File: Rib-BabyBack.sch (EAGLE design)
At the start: 30 parts, among them IC1 REG1117, SW1 DPDT

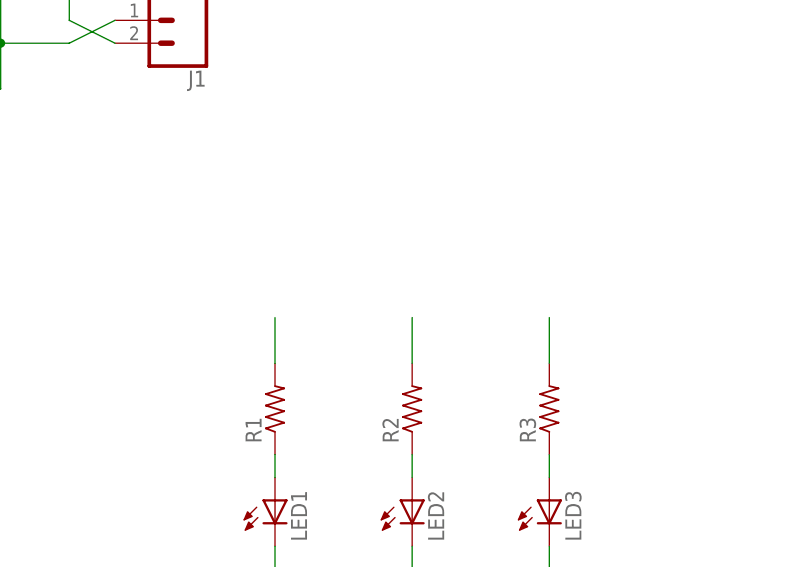
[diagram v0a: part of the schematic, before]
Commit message: Resolved issue 38
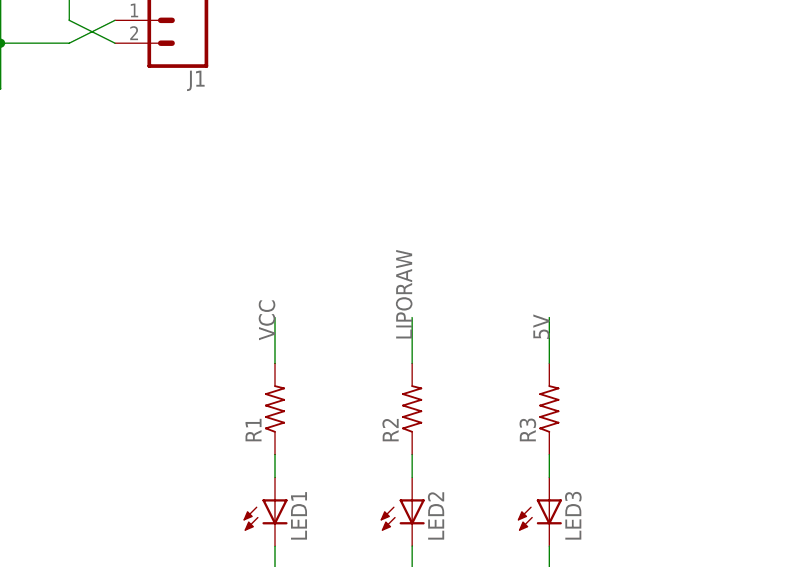
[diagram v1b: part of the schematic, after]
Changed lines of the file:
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@@
 <pinref part="R1" gate="G$1" pin="2"/>
 <wire x1="96.52" y1="-96.52" x2="96.52" y2="-91.44" width="0.1524" layer="91"/>
+<label x="96.52" y="-93.98" size="1.778" layer="95" rot="R90"/>
 </segment>
 </net>
@@
 <pinref part="R3" gate="G$1" pin="2"/>
 <wire x1="127" y1="-96.52" x2="127" y2="-91.44" width="0.1524" layer="91"/>
+<label x="127" y="-93.98" size="1.778" layer="95" rot="R90"/>
 </segment>
 <segment>
@@
 <pinref part="R2" gate="G$1" pin="2"/>
 <wire x1="111.76" y1="-96.52" x2="111.76" y2="-91.44" width="0.1524" layer="91"/>
+<label x="111.76" y="-93.98" size="1.778" layer="95" rot="R90"/>
 </segment>
 </net>

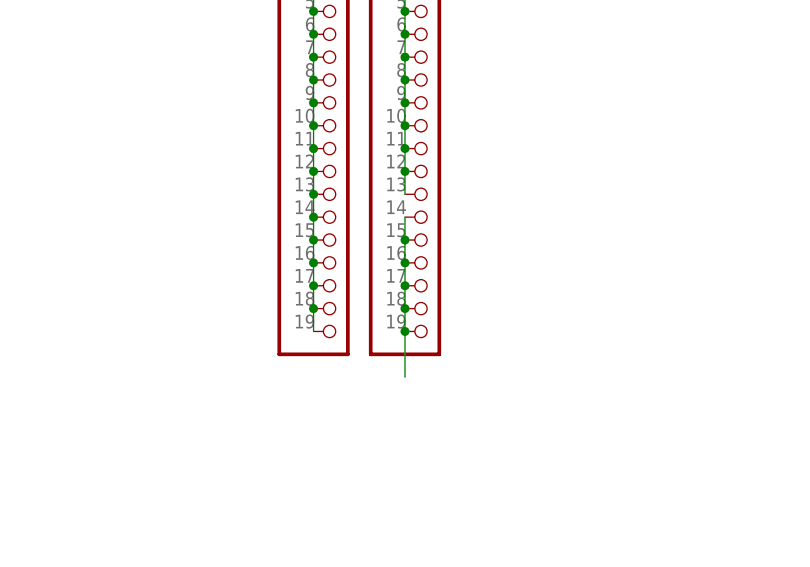
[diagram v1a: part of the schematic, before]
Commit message: changed 5v rail
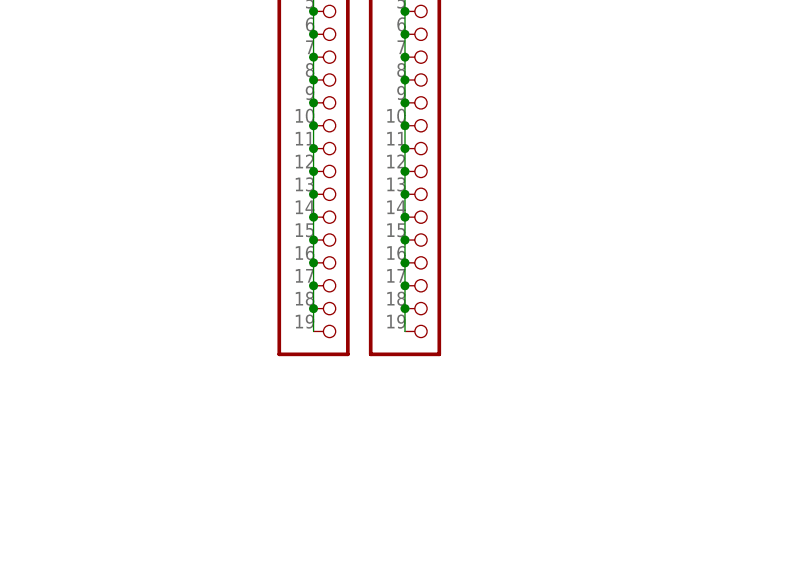
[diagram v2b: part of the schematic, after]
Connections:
- net 5V: no longer JP4.14, JP4.15, JP4.16, JP4.17, JP4.18, JP4.19
- net SENSORV: now also JP4.14, JP4.15, JP4.16, JP4.17, JP4.18, JP4.19
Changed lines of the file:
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@@
 <?xml version="1.0" encoding="utf-8"?>
 <!DOCTYPE eagle SYSTEM "eagle.dtd">
-<eagle version="8.6.3">
+<eagle version="9.1.0">
 <drawing>
 <settings>
@@
 <wire x1="-76.2" y1="-210.82" x2="-76.2" y2="-215.9" width="0.1524" layer="91"/>
 </segment>
-<segment>
-<pinref part="JP4" gate="G$1" pin="15"/>
-<pinref part="JP4" gate="G$1" pin="19"/>
-<wire x1="-22.86" y1="-91.44" x2="-22.86" y2="-93.98" width="0.1524" layer="91"/>
-<wire x1="-22.86" y1="-93.98" x2="-22.86" y2="-96.52" width="0.1524" layer="91"/>
-<wire x1="-22.86" y1="-96.52" x2="-22.86" y2="-99.06" width="0.1524" layer="91"/>
-<wire x1="-22.86" y1="-99.06" x2="-22.86" y2="-101.6" width="0.1524" layer="91"/>
-<wire x1="-22.86" y1="-101.6" x2="-22.86" y2="-106.68" width="0.1524" layer="91"/>
-<junction x="-22.86" y="-101.6"/>
-<pinref part="JP4" gate="G$1" pin="16"/>
-<junction x="-22.86" y="-93.98"/>
-<pinref part="JP4" gate="G$1" pin="17"/>
-<junction x="-22.86" y="-96.52"/>
-<pinref part="JP4" gate="G$1" pin="18"/>
-<junction x="-22.86" y="-99.06"/>
-<pinref part="JP4" gate="G$1" pin="14"/>
-<wire x1="-22.86" y1="-88.9" x2="-22.86" y2="-91.44" width="0.1524" layer="91"/>
-<junction x="-22.86" y="-91.44"/>
-</segment>
 </net>
 <net name="LIPORAW" class="0">
@@
 <junction x="-22.86" y="-83.82"/>
 <pinref part="JP4" gate="G$1" pin="13"/>
-</segment>
-<segment>
+<pinref part="JP4" gate="G$1" pin="15"/>
+<pinref part="JP4" gate="G$1" pin="19"/>
+<wire x1="-22.86" y1="-91.44" x2="-22.86" y2="-93.98" width="0.1524" layer="91"/>
+<wire x1="-22.86" y1="-93.98" x2="-22.86" y2="-96.52" width="0.1524" layer="91"/>
+<wire x1="-22.86" y1="-96.52" x2="-22.86" y2="-99.06" width="0.1524" layer="91"/>
+<wire x1="-22.86" y1="-99.06" x2="-22.86" y2="-101.6" width="0.1524" layer="91"/>
+<pinref part="JP4" gate="G$1" pin="16"/>
+<junction x="-22.86" y="-93.98"/>
+<pinref part="JP4" gate="G$1" pin="17"/>
+<junction x="-22.86" y="-96.52"/>
+<pinref part="JP4" gate="G$1" pin="18"/>
+<junction x="-22.86" y="-99.06"/>
+<pinref part="JP4" gate="G$1" pin="14"/>
+<wire x1="-22.86" y1="-88.9" x2="-22.86" y2="-91.44" width="0.1524" layer="91"/>
+<junction x="-22.86" y="-91.44"/>
+<wire x1="-22.86" y1="-86.36" x2="-22.86" y2="-88.9" width="0.1524" layer="91"/>
+<junction x="-22.86" y="-86.36"/>
+<junction x="-22.86" y="-88.9"/>
+</segment>
+<segment>
